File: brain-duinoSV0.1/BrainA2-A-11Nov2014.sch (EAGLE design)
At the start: 30 parts, among them IC1 OPA2111KP, IC4 OP2177ARMZ

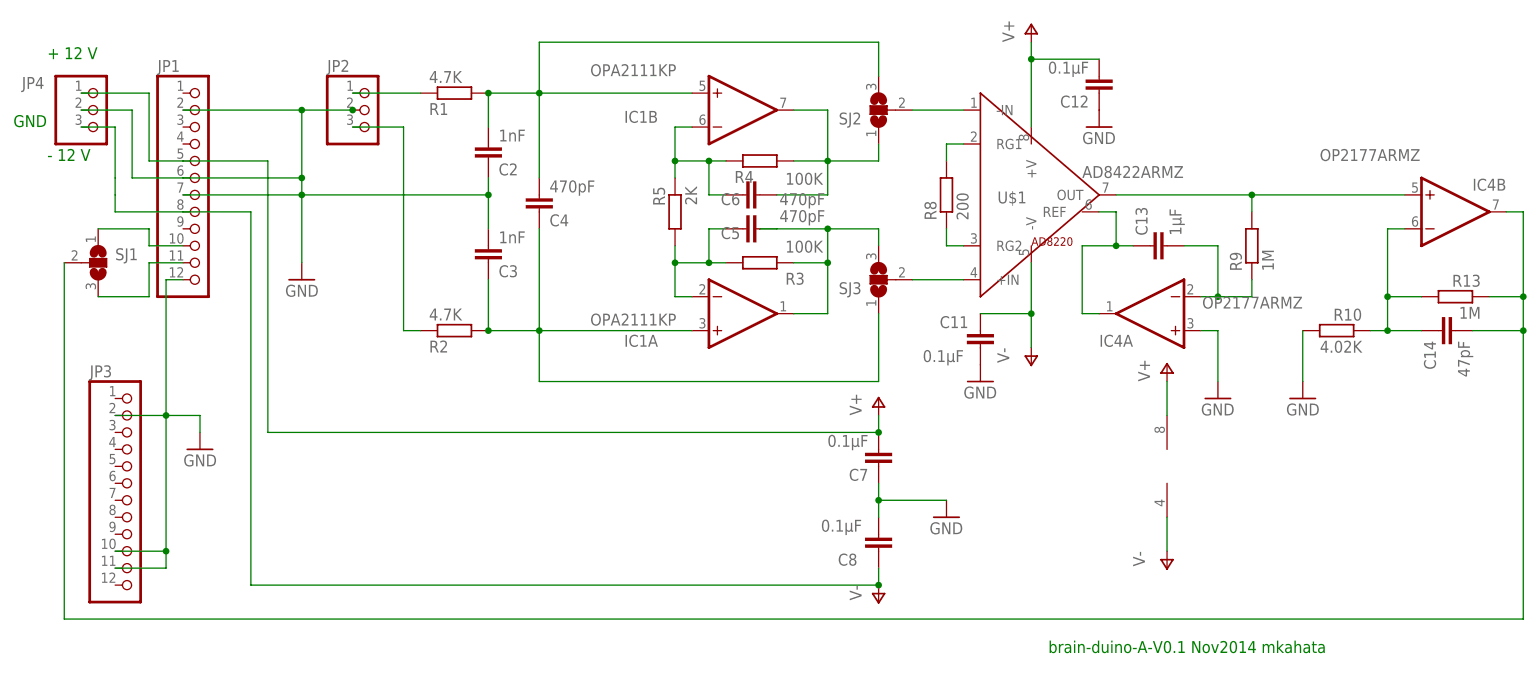
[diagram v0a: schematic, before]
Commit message: BrainA2-A: Getting rid of some schematic level ERC errors and warnings Renamed U$1 to IC8
Signed-off-by: Christoph Maier <cm.hardware.software.elsewhere@gmail.com>
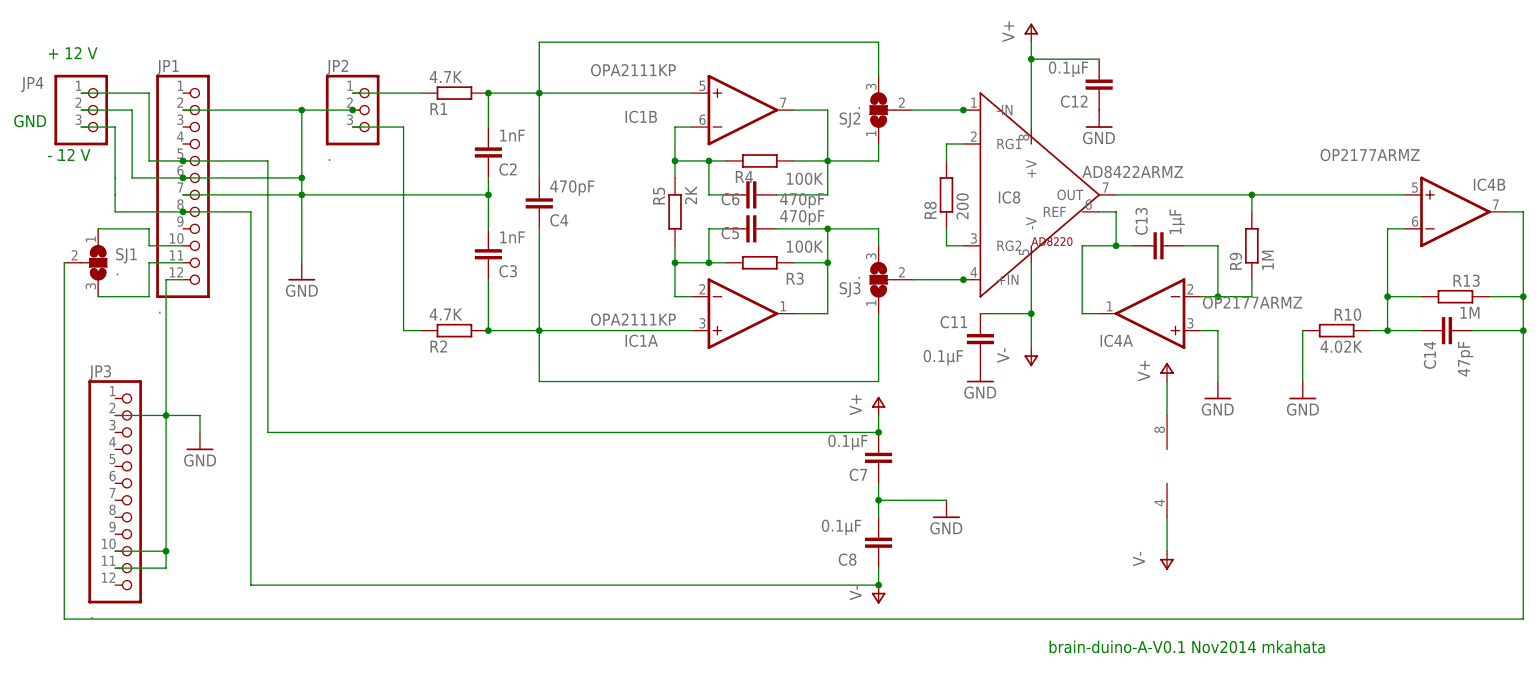
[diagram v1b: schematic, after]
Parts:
- JP1, JP2, JP3, JP4, SJ1, SJ2, SJ3: value (none) -> .
- renumbered U$1 to IC8
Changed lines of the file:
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@@
 <?xml version="1.0" encoding="utf-8"?>
 <!DOCTYPE eagle SYSTEM "eagle.dtd">
-<eagle version="7.1.0">
+<eagle version="6.5.0">
 <drawing>
 <settings>
@@
 <part name="P+4" library="supply1" deviceset="V+" device=""/>
 <part name="P-4" library="supply1" deviceset="V-" device=""/>
-<part name="U$1" library="MKH" deviceset="AD8220" device="" value="AD8422ARMZ"/>
+<part name="IC8" library="MKH" deviceset="AD8220" device="" value="AD8422ARMZ"/>
 <part name="C12" library="rcl" deviceset="C-EU" device="C0603" value="0.1µF"/>
 <part name="GND9" library="supply1" deviceset="GND" device=""/>
@@
 <part name="P-6" library="supply1" deviceset="V-" device=""/>
 <part name="P+5" library="supply1" deviceset="V+" device=""/>
-<part name="JP1" library="pinhead" deviceset="PINHD-1X12" device=""/>
-<part name="JP3" library="pinhead" deviceset="PINHD-1X12" device=""/>
+<part name="JP1" library="pinhead" deviceset="PINHD-1X12" device="" value="."/>
+<part name="JP3" library="pinhead" deviceset="PINHD-1X12" device="" value="."/>
 <part name="GND3" library="supply1" deviceset="GND" device=""/>
-<part name="JP2" library="pinhead" deviceset="PINHD-1X3" device=""/>
-<part name="SJ1" library="jumper" deviceset="SJ2W" device=""/>
-<part name="SJ2" library="jumper" deviceset="SJ2W" device=""/>
-<part name="SJ3" library="jumper" deviceset="SJ2W" device=""/>
-<part name="JP4" library="pinhead" deviceset="PINHD-1X3" device=""/>
+<part name="JP2" library="pinhead" deviceset="PINHD-1X3" device="" value="."/>
+<part name="SJ1" library="jumper" deviceset="SJ2W" device="" value="."/>
+<part name="SJ2" library="jumper" deviceset="SJ2W" device="" value="."/>
+<part name="SJ3" library="jumper" deviceset="SJ2W" device="" value="."/>
+<part name="JP4" library="pinhead" deviceset="PINHD-1X3" device="" value="."/>
 </parts>
 <sheets>
@@
 <instance part="P+4" gate="1" x="180.34" y="129.54"/>
 <instance part="P-4" gate="1" x="180.34" y="78.74"/>
-<instance part="U$1" gate="G$1" x="180.34" y="104.14" smashed="yes">
+<instance part="IC8" gate="G$1" x="180.34" y="104.14" smashed="yes">
 <attribute name="NAME" x="175.26" y="102.87" size="1.778" layer="95"/>
 <attribute name="VALUE" x="187.96" y="106.68" size="1.778" layer="96"/>
@@
 <wire x1="45.72" y1="116.84" x2="38.1" y2="116.84" width="0.1524" layer="91"/>
 <pinref part="JP4" gate="A" pin="2"/>
+<junction x="53.34" y="106.68"/>
 </segment>
 <segment>
@@
 <wire x1="66.04" y1="68.58" x2="66.04" y2="109.22" width="0.1524" layer="91"/>
 <junction x="157.48" y="68.58"/>
+<pinref part="JP4" gate="A" pin="1"/>
+<wire x1="48.26" y1="109.22" x2="48.26" y2="119.38" width="0.1524" layer="91"/>
+<wire x1="48.26" y1="119.38" x2="38.1" y2="119.38" width="0.1524" layer="91"/>
 <pinref part="JP1" gate="G$1" pin="5"/>
-<wire x1="53.34" y1="109.22" x2="66.04" y2="109.22" width="0.1524" layer="91"/>
-<wire x1="53.34" y1="109.22" x2="48.26" y2="109.22" width="0.1524" layer="91"/>
-<wire x1="48.26" y1="109.22" x2="48.26" y2="119.38" width="0.1524" layer="91"/>
-<pinref part="JP4" gate="A" pin="1"/>
-<wire x1="48.26" y1="119.38" x2="38.1" y2="119.38" width="0.1524" layer="91"/>
+<wire x1="48.26" y1="109.22" x2="53.34" y2="109.22" width="0.1524" layer="91"/>
+<wire x1="66.04" y1="109.22" x2="53.34" y2="109.22" width="0.1524" layer="91"/>
+<junction x="53.34" y="109.22"/>
 </segment>
 <segment>
@@
 <wire x1="190.5" y1="124.46" x2="180.34" y2="124.46" width="0.1524" layer="91"/>
 <pinref part="P+4" gate="1" pin="V+"/>
-<pinref part="U$1" gate="G$1" pin="+V"/>
+<pinref part="IC8" gate="G$1" pin="+V"/>
 <wire x1="180.34" y1="124.46" x2="180.34" y2="114.3" width="0.1524" layer="91"/>
 <junction x="180.34" y="124.46"/>
@@
 <wire x1="43.18" y1="106.68" x2="43.18" y2="114.3" width="0.1524" layer="91"/>
 <wire x1="43.18" y1="104.14" x2="43.18" y2="106.68" width="0.1524" layer="91"/>
+<junction x="53.34" y="101.6"/>
 </segment>
 <segment>
@@
 <wire x1="180.34" y1="86.36" x2="180.34" y2="81.28" width="0.1524" layer="91"/>
 <pinref part="P-4" gate="1" pin="V-"/>
-<pinref part="U$1" gate="G$1" pin="-V"/>
+<pinref part="IC8" gate="G$1" pin="-V"/>
 <wire x1="180.34" y1="93.98" x2="180.34" y2="86.36" width="0.1524" layer="91"/>
 <junction x="180.34" y="86.36"/>
@@
 <pinref part="R3" gate="G$1" pin="2"/>
 <wire x1="144.78" y1="93.98" x2="149.86" y2="93.98" width="0.1524" layer="91"/>
-<wire x1="139.7" y1="99.06" x2="142.24" y2="99.06" width="0.1524" layer="91"/>
 <wire x1="142.24" y1="99.06" x2="149.86" y2="99.06" width="0.1524" layer="91"/>
 <wire x1="149.86" y1="99.06" x2="149.86" y2="93.98" width="0.1524" layer="91"/>
@@
 <wire x1="170.18" y1="96.52" x2="167.64" y2="96.52" width="0.1524" layer="91"/>
 <wire x1="167.64" y1="96.52" x2="167.64" y2="99.06" width="0.1524" layer="91"/>
-<pinref part="U$1" gate="G$1" pin="RG2"/>
+<pinref part="IC8" gate="G$1" pin="RG2"/>
 </segment>
 </net>
@@
 <wire x1="167.64" y1="109.22" x2="167.64" y2="111.76" width="0.1524" layer="91"/>
 <wire x1="167.64" y1="111.76" x2="170.18" y2="111.76" width="0.1524" layer="91"/>
-<pinref part="U$1" gate="G$1" pin="RG1"/>
+<pinref part="IC8" gate="G$1" pin="RG1"/>
 </segment>
 </net>
@@
 <wire x1="193.04" y1="104.14" x2="213.36" y2="104.14" width="0.1524" layer="91"/>
 <junction x="213.36" y="104.14"/>
-<pinref part="U$1" gate="G$1" pin="OUT"/>
+<pinref part="IC8" gate="G$1" pin="OUT"/>
 </segment>
 </net>
@@
 <wire x1="187.96" y1="86.36" x2="187.96" y2="96.52" width="0.1524" layer="91"/>
 <wire x1="187.96" y1="96.52" x2="193.04" y2="96.52" width="0.1524" layer="91"/>
-<pinref part="U$1" gate="G$1" pin="REF"/>
+<pinref part="IC8" gate="G$1" pin="REF"/>
 <wire x1="193.04" y1="96.52" x2="195.58" y2="96.52" width="0.1524" layer="91"/>
 <wire x1="190.5" y1="101.6" x2="193.04" y2="101.6" width="0.1524" layer="91"/>
@@
 <net name="N$14" class="0">
 <segment>
-<pinref part="U$1" gate="G$1" pin="-IN"/>
-<pinref part="U$1" gate="G$1" pin="-IN"/>
+<pinref part="IC8" gate="G$1" pin="-IN"/>
+<pinref part="IC8" gate="G$1" pin="-IN"/>
 <pinref part="SJ2" gate="G$1" pin="2"/>
-<wire x1="162.56" y1="116.84" x2="170.18" y2="116.84" width="0.1524" layer="91"/>
+<wire x1="170.18" y1="116.84" x2="162.56" y2="116.84" width="0.1524" layer="91"/>
+<junction x="170.18" y="116.84"/>
 </segment>
 </net>
 <net name="N$15" class="0">
 <segment>
-<pinref part="U$1" gate="G$1" pin="+IN"/>
-<pinref part="U$1" gate="G$1" pin="+IN"/>
+<pinref part="IC8" gate="G$1" pin="+IN"/>
+<pinref part="IC8" gate="G$1" pin="+IN"/>
 <pinref part="SJ3" gate="G$1" pin="2"/>
-<wire x1="162.56" y1="91.44" x2="170.18" y2="91.44" width="0.1524" layer="91"/>
-</segment>
-</net>
+<wire x1="170.18" y1="91.44" x2="162.56" y2="91.44" width="0.1524" layer="91"/>
+<junction x="170.18" y="91.44"/>
+</segment>
+</net>
